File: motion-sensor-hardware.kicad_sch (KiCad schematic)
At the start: 39 parts, among them J1 MX128-2.54-04P-GN01-Cu-Y-A, J2 MX128-2.54-02P-GN01-Cu-Y-A, J3 PZ254V-11-03P, J5 TYPE-C 16PIN 2MD(073), Q1 BSS138, Q2 XR30P10L, SW1 TS-1088-AR02016, SW2 TS-1088-AR02016, U1 ESP32-C3-MINI-1-N4, U2 LD2410C, U5 ASSR-1218

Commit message: Ready to restart work!
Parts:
- removed Q1: BSS138, Package_TO_SOT_SMD:SOT-23, symbol Transistor_FET:BSS138
- removed R13: 10k, Capacitor_SMD:C_0805_2012Metric, symbol Device:R

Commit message: Schematic complete (I think)
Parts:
- removed C10: 10u, Capacitor_SMD:C_0805_2012Metric, symbol Device:C
- removed C7: 1u, Capacitor_SMD:C_0805_2012Metric, symbol Device:C
- removed C8, C9: 0.1u, Capacitor_SMD:C_0805_2012Metric, symbol Device:C
- removed D1, D2: LESD5D5.0CT1G, Diode_SMD:D_SOD-523, symbol Device:D_TVS
- removed D4, D6: P6SMB6.8CA/TR13, Diode_SMD:D_SMB_Handsoldering, symbol Device:D_TVS
- removed D8: BZT52C15S, Diode_SMD:D_SOD-323, symbol Device:D_Zener
- removed Q2: XR30P10L, Package_TO_SOT_SMD:SOT-23, symbol Transistor_FET:Q_PMOS_GSD
- removed R1, R5: 5.1k, Capacitor_SMD:C_0805_2012Metric, symbol Device:R
- removed R10, R9: 0, Capacitor_SMD:C_0805_2012Metric, symbol Device:R
- removed R11, R15, R6, R7, R8: 10k, Capacitor_SMD:C_0805_2012Metric, symbol Device:R
- removed R12: 330, Resistor_SMD:R_0805_2012Metric_Pad1.20x1.40mm_HandSolder, symbol Device:R
- removed R14: 100, Capacitor_SMD:C_0805_2012Metric, symbol Device:R
- added C1: 10uF, Capacitor_SMD:C_0603_1608Metric, symbol !Capacitor-0603:10uF_X5R_10V
- added C14, C8, C9: 100nF, Capacitor_SMD:C_0603_1608Metric, symbol !Capacitor-0603:100nF_X7R_50V
- added C7: 1uF, Capacitor_SMD:C_0603_1608Metric, symbol !Capacitor-0603:1uF_X5R_50V
- added D1: BZT52C10S, Diode_SMD:D_SOD-323, symbol !Diode-Zener:BZT52C10S
- added D2, D3: SMF6.5CA, Diode_SMD:D_SOD-123F, symbol !Circuit Protection-ESD+TVS:SMF6.5CA
- added Q1: AO3401A, Package_TO_SOT_SMD:TSOT-23, symbol !MOSFET:AO3401A
- added R1, R5: 5.1kΩ, Resistor_SMD:R_0603_1608Metric, symbol !Resistor-0603:5.1kΩ
- added R10, R9: 0Ω, Resistor_SMD:R_0603_1608Metric, symbol !Resistor-0603:0Ω
- added R11, R15, R6, R7, R8: 10kΩ, Resistor_SMD:R_0603_1608Metric, symbol !Resistor-0603:10kΩ
- added R12: 330Ω, Resistor_SMD:R_0603_1608Metric, symbol !Resistor-0603:330Ω
- added R14: 100Ω, Resistor_SMD:R_0603_1608Metric, symbol !Resistor-0603:100Ω
- added U6: USBLC6-2SC6, Package_TO_SOT_SMD:SOT-23-6, symbol !Circuit Protection-ESD+TVS:USBLC6-2SC6
- added U7: SN74LV1T125DCK, Package_TO_SOT_SMD:SOT-353_SC-70-5, symbol !Logic-Buffer:SN74LV1T125DCK
- D5: symbol Device:D_TVS -> !Circuit Protection-ESD+TVS:P6SMB24CA-E3/52
- D7: value WS2812B -> WS2812B-HS01/W; symbol LED:WS2812B -> !Optoelectronics-LED:WS2812B-HS01/W; JLCPCB (none) -> C22371521
- F1: symbol Device:Polyfuse -> !Circuit Protection-Resettable Fuse:JK-nSMD100/16V
- J1: value MX128-2.54-04P-GN01-Cu-Y-A -> MX128-2.54-04P; symbol Connector:Screw_Terminal_01x04 -> !Connectors-Screw:MX128-2.54-04P
- J2: value MX128-2.54-02P-GN01-Cu-Y-A -> MX128-2.54-02P; symbol Connector:Screw_Terminal_01x02 -> !Connectors-Screw:MX128-2.54-02P; JLCPCB C5188442 -> C5188442
- J3: symbol Connector_Generic:Conn_01x03 -> !Connectors-Header:PZ254V-11-03P; now not fitted
- J5: symbol Connector:USB_C_Receptacle_USB2.0_16P -> !Connectors-USB:USB_C_Receptacle_USB2.0_16P
- SW1, SW2: symbol Switch:SW_Push -> !Switch:TS-1088-AR02016
- U1: footprint RF_Module:ESP32-C6-MINI-1 -> !RF_Modules:ESP32-C6-MINI-1; symbol motion-sensor-syms:ESP32-C3-MINI-1 -> !RF Modules:ESP32-C3-MINI-1
- U2: footprint HLK:LD2410C -> !Sensors:LD2410C; symbol motion-sensor-syms:LD2410C -> !Sensors:LD2410C
- U5: symbol Relay_SolidState:ASSR-1218 -> !Optoisolator-SSR:ASSR-1218; JLCPCB (none) -> C6747780
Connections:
- net +3.3V: now also C1.1, C8.1, R11.1, R6.1, R7.1, R8.1
- net +5V: now also C14.1, C9.1, U7.5 (VCC)
- net CTL_SW1: now also D2.2 (A2)
- net CTL_SW2: now also D2.1 (A1)
- net GND: now also C1.2, C14.2, C7.2, C8.2, C9.2, D3.1 (A1), R1.2, R15.2, R5.2, U6.2 (GND), U7.1 (~{OE}), U7.3 (GND)
- net LED: now also U7.2 (A)
- net STAT_SW: now also D3.2 (A2)
- net SWON: now also R12.1
- net USB+: now also R10.2
- net USB-: now also R9.2
- net USB1+: now also R10.1, U6.4 (I/O2); no longer J5.A6 (D+), J5.B6 (D+)
- net USB1-: now also R9.1, U6.6 (I/O1); no longer J5.A7 (D-), J5.B7 (D-)
- net VIN: now also D1.1 (K), Q1.2 (S)
- net at J5.A5 (CC1): now also R1.1
- net at SW2.2, U1.8 (EN/CHIP_PU): now also C7.1, R6.2
- net at D7.4 (DIN): now also U7.4 (Y)
- net at U1.22 (GPIO8): now also R8.2
- net at SW1.2, U1.23 (GPIO9): now also R11.2
- net at U1.5 (GPIO2/ADC1_CH2): now also R7.2
- net at J5.B5 (CC2): now also R5.1
- net at D5.2 (A2), F1.2: now also Q1.3 (D)
- net at U5.1: now also R12.2
- net at J5.A4 (VBUS), J5.A9 (VBUS), J5.B4 (VBUS)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: now also U6.5 (VBUS)
- new net: Q1.1 (G), R14.1
- new net: D1.2 (A), R14.2, R15.1
- new net: J5.A7 (D-), J5.B7 (D-), U6.1 (I/O1)
- new net: J5.A6 (D+), J5.B6 (D+), U6.3 (I/O2)
- no-connect marks 6 -> 5
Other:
- note added: "V_{in} is 16 V max"
- moved on the sheet: SW1, SW2

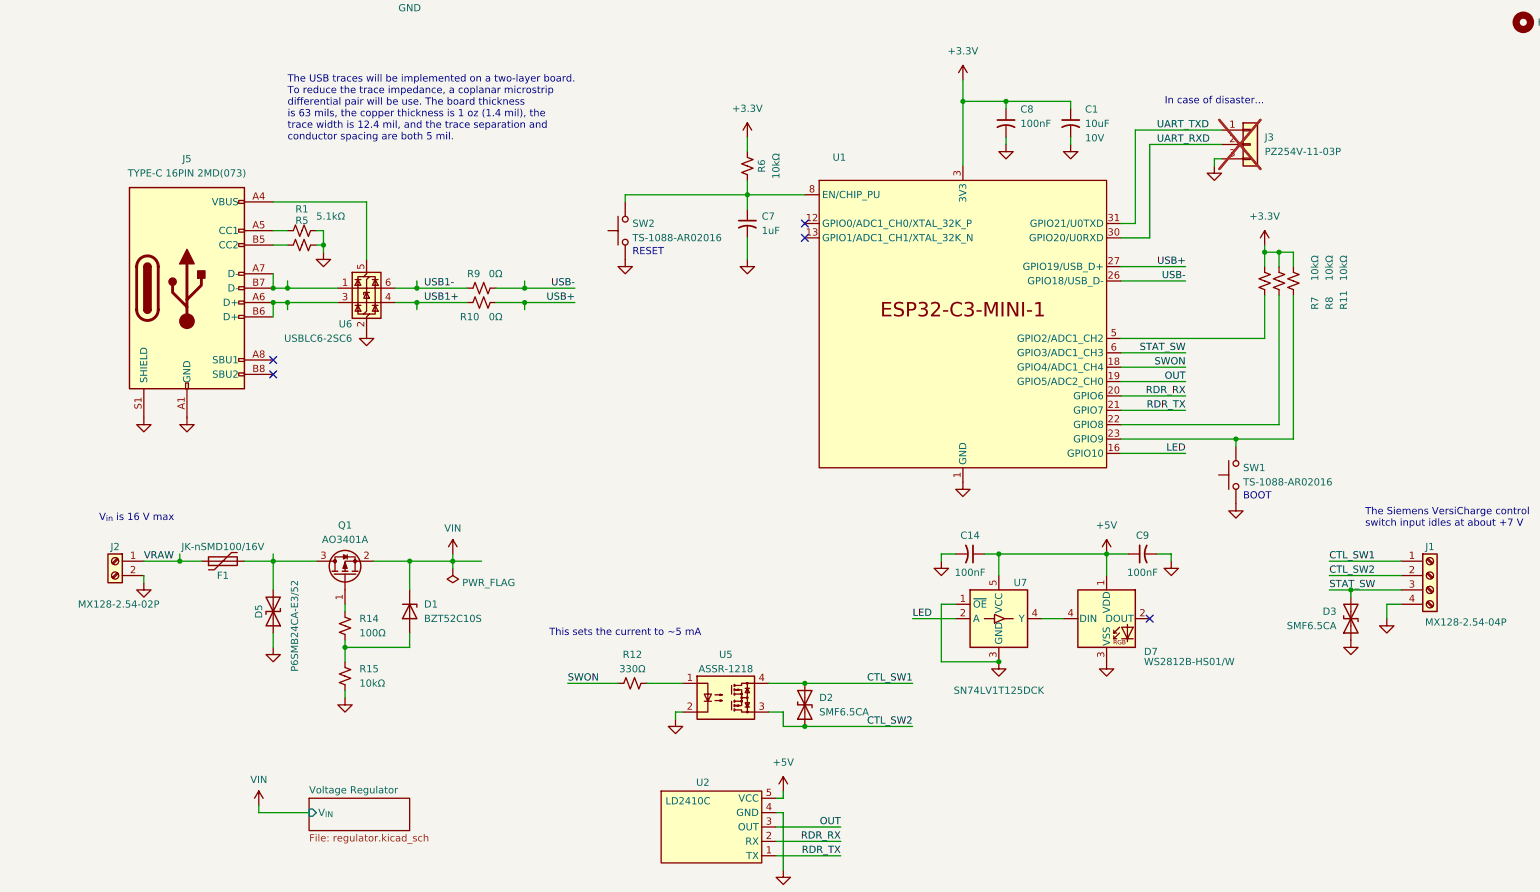
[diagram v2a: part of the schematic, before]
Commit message: Split the two ground planes
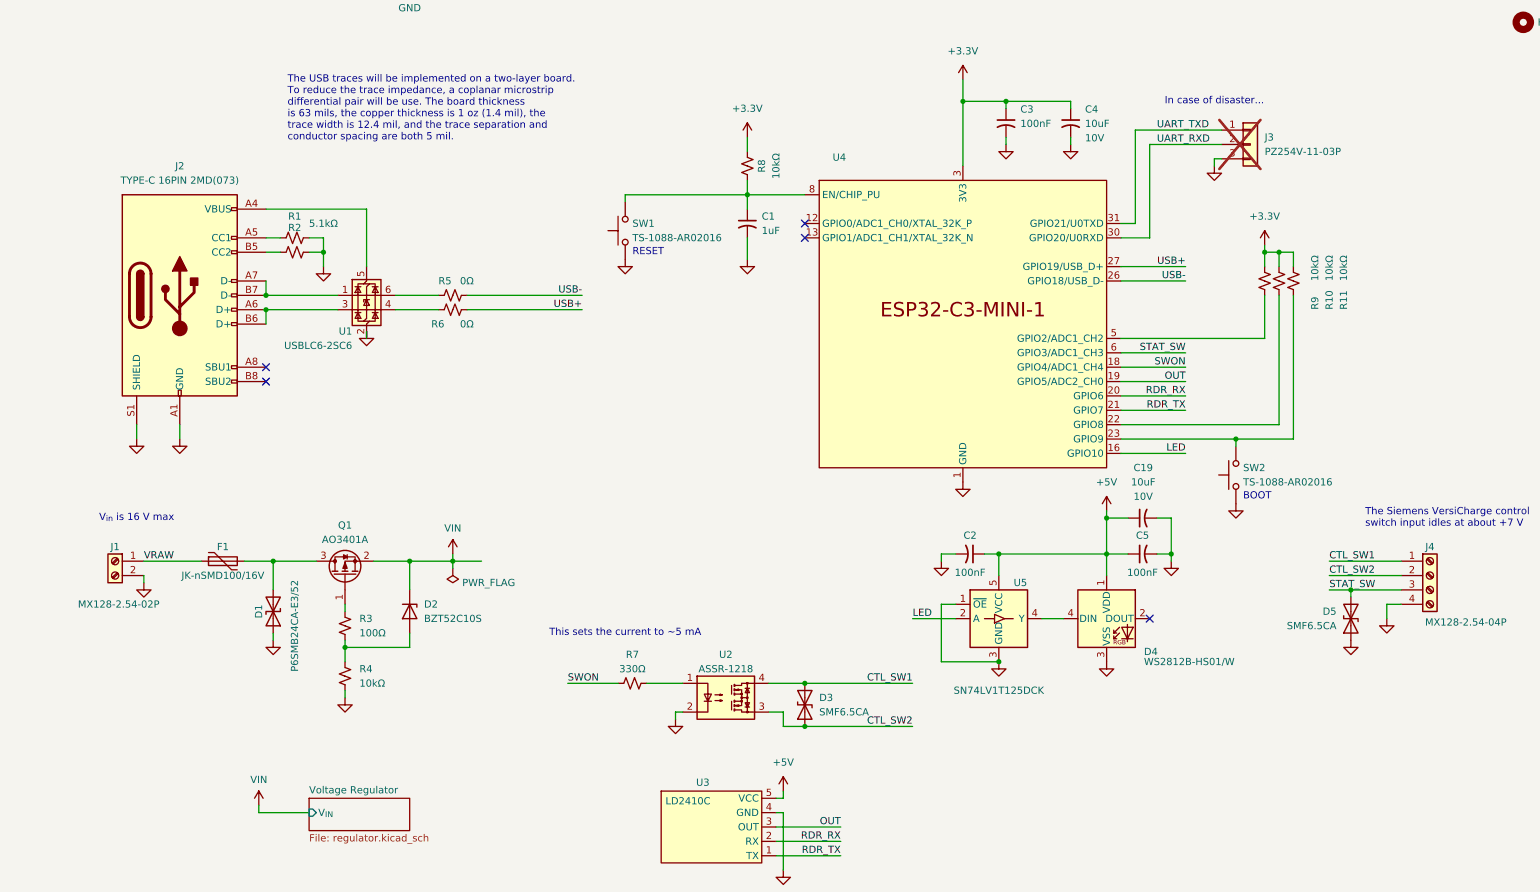
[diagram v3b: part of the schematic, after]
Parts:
- added C19: 10uF, Capacitor_SMD:C_0603_1608Metric, symbol !Capacitor-0603:10uF_X5R_10V
- J1: renamed from J2; footprint My_Connectors:MX300-5.0-02P -> !Connectors:MX128-2.54-02P
- J4: renamed from J1; footprint (none) -> !Connectors:MX128-2.54-04P
- renumbered C7 to C1, C14 to C2, C8 to C3, C1 to C4, C9 to C5, D5 to D1, D1 to D2, D2 to D3, D7 to D4, D3 to D5, J5 to J2, R8 to R10, R5 to R2, R14 to R3, R15 to R4, R9 to R5, R10 to R6, R12 to R7, R6 to R8, R7 to R9, SW2 to SW1, SW1 to SW2, U6 to U1, U5 to U2, U2 to U3, U1 to U4, U7 to U5
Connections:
- net +5V: now also C19.1
- net GND: now also C19.2
- net USB1+: no longer names the net of R6.1, U1.4 (I/O2)
- net USB1-: no longer names the net of R5.1, U1.6 (I/O1)
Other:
- moved on the sheet: J2, R1, R2, R5, R6, U1

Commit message: Rev B Submitted
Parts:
- removed D1: P6SMB24CA-E3/52, Diode_SMD:D_SMB, symbol !Circuit Protection-ESD+TVS:P6SMB24CA-E3/52
- added D1: SMBJ16CA, Diode_SMD:D_SMB, symbol !Circuit Protection-ESD+TVS:SMBJ16CA
- C1: JLCPCB C15849 -> (none); JLCPCB PN (none) -> C15849
- C19, C4: JLCPCB C19702 -> (none); JLCPCB PN (none) -> C19702
- C2, C3, C5: JLCPCB C14663 -> (none); JLCPCB PN (none) -> C14663
- D2: JLCPCB C19077446 -> (none); JLCPCB PN (none) -> C19077446
- D3, D5: JLCPCB C19077501 -> (none); JLCPCB PN (none) -> C19077501
- D4: JLCPCB C22371521 -> (none); JLCPCB PN (none) -> C22371521
- F1: JLCPCB C2830246 -> (none); JLCPCB PN (none) -> C2830246
- J1: FT Rotation Offset (none) -> 180; JLCPCB C5188442 -> (none); JLCPCB PN (none) -> C5188442
- J2: FT Origin (none) -> Center; JLCPCB C2765186 -> (none); JLCPCB PN (none) -> C2765186
- J3: JLCPCB C2937625 -> (none); JLCPCB PN (none) -> C2937625
- J4: FT Rotation Offset (none) -> 180; JLCPCB C5188444 -> (none); JLCPCB PN (none) -> C5188444
- Q1: JLCPCB C15127 -> (none); JLCPCB PN (none) -> C15127
- R1, R2: JLCPCB C23186 -> (none); JLCPCB PN (none) -> C23186
- R10, R11, R4, R8, R9: JLCPCB C25804 -> (none); JLCPCB PN (none) -> C25804
- R3: JLCPCB C22775 -> (none); JLCPCB PN (none) -> C22775
- R5, R6: JLCPCB C21189 -> (none); JLCPCB PN (none) -> C21189
- R7: JLCPCB C23138 -> (none); JLCPCB PN (none) -> C23138
- SW1, SW2: JLCPCB C720477 -> (none); JLCPCB PN (none) -> C720477
- U1: FT Rotation Offset (none) -> 90; JLCPCB C7519 -> (none); JLCPCB PN (none) -> C7519
- U2: FT Rotation Offset (none) -> 90; JLCPCB C6747780 -> (none); JLCPCB PN (none) -> C6747780
- U3: JLCPCB C19723500 -> (none); JLCPCB PN (none) -> C19723500
- U4: JLCPCB C2838502 -> (none); JLCPCB PN (none) -> C2838502
- U5: FT Rotation Offset (none) -> 180; JLCPCB C75925 -> (none); JLCPCB PN (none) -> C75925
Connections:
- net GND: now also D1.1 (A1)
- net at F1.2, Q1.3 (D): now also D1.2 (A2)
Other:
- title: (none) -> Motion Sensor/Charge Control

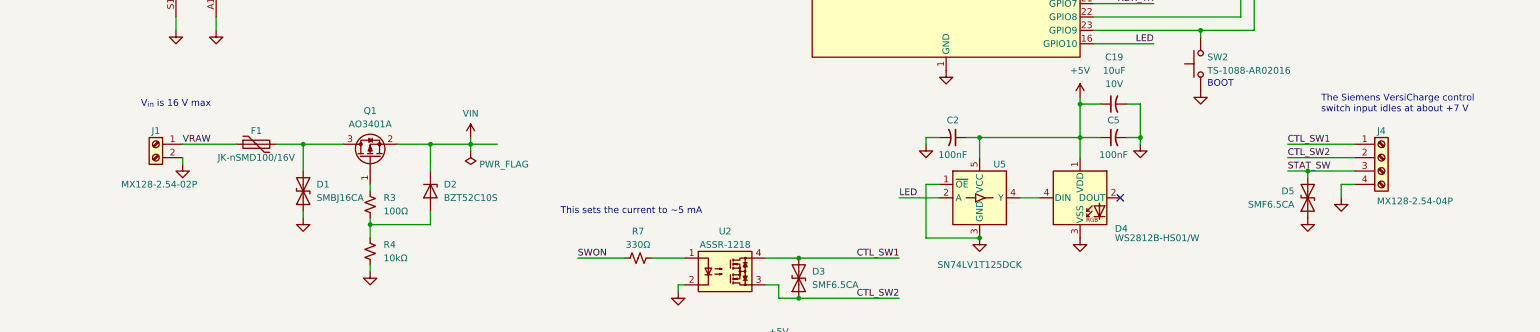
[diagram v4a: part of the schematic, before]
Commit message: Fixed screw term pin 1 issue
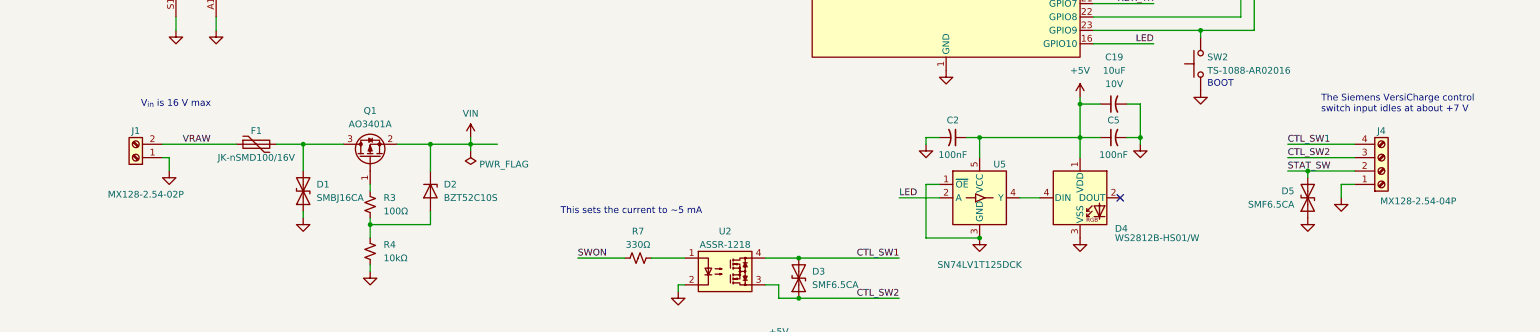
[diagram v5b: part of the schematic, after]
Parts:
- SW1, SW2: footprint Button_Switch_SMD:SW_Push_SPST_NO_Alps_SKRK -> !Switches:SW_TS-1088-xx020xx_XUNPU
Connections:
- net CTL_SW1: now also J4.4 (Pin_4); no longer J4.1 (Pin_1)
- net CTL_SW2: now also J4.3 (Pin_3); no longer J4.2 (Pin_2)
- net GND: now also J1.1 (Pin_1), J4.1 (Pin_1); no longer J1.2 (Pin_2), J4.4 (Pin_4)
- net STAT_SW: now also J4.2 (Pin_2); no longer J4.3 (Pin_3)
- net VRAW: now also J1.2 (Pin_2); no longer J1.1 (Pin_1)
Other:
- moved on the sheet: J1
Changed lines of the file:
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@@
 	(wire
 		(pts
+			(xy 25.4 138.43) (xy 39.37 138.43)
+		)
+		(stroke
+			(width 0)
+			(type default)
+		)
+	)
+	(wire
+		(pts
 			(xy 201.93 104.14) (xy 213.36 104.14)
 		)
@@
 	(wire
 		(pts
-			(xy 29.21 140.97) (xy 29.21 142.24)
-		)
-		(stroke
-			(width 0)
-			(type default)
-		)
-	)
-	(wire
-		(pts
 			(xy 64.77 146.05) (xy 64.77 147.32)
 		)
@@
 	(wire
 		(pts
-			(xy 142.24 180.34) (xy 142.24 179.07)
+			(xy 25.4 140.97) (xy 26.67 140.97)
 		)
 		(stroke
@@
 	(wire
 		(pts
-			(xy 29.21 138.43) (xy 39.37 138.43)
+			(xy 142.24 180.34) (xy 142.24 179.07)
 		)
 		(stroke
@@
 	(wire
 		(pts
+			(xy 26.67 140.97) (xy 26.67 143.51)
+		)
+		(stroke
+			(width 0)
+			(type default)
+		)
+	)
+	(wire
+		(pts
 			(xy 227.33 83.82) (xy 229.87 83.82)
 		)
@@
 			)
 		)
-		(property "Footprint" "Button_Switch_SMD:SW_Push_SPST_NO_Alps_SKRK"
+		(property "Footprint" "!Switches:SW_TS-1088-xx020xx_XUNPU"
 			(at 109.22 80.01 0)
 			(effects
@@
 	(symbol
 		(lib_id "!Connectors-Screw:MX128-2.54-02P")
-		(at 24.13 138.43 0)
-		(mirror y)
+		(at 20.32 140.97 180)
 		(unit 1)
 		(exclude_from_sim no)
@@
 		(dnp no)
 		(property "Reference" "J1"
-			(at 24.13 135.89 0)
+			(at 20.32 135.89 0)
 			(effects
 				(font
@@
 		)
 		(property "Value" "MX128-2.54-02P"
-			(at 24.765 146.05 0)
+			(at 22.225 147.955 0)
 			(effects
 				(font
@@
 		)
 		(property "Footprint" "!Connectors:MX128-2.54-02P"
-			(at 24.13 138.43 0)
+			(at 20.32 140.97 0)
 			(effects
 				(font
@@
 		)
 		(property "Datasheet" "https://jlcpcb.com/api/file/downloadByFileSystemAccessId/8604752379715997696"
-			(at 24.13 138.43 0)
+			(at 20.32 140.97 0)
 			(effects
 				(font
@@
 		)
 		(property "Description" "Screw Term Block, 2 Pos, 2.54 mm"
-			(at 24.13 138.43 0)
+			(at 20.32 140.97 0)
 			(effects
 				(font
@@
 		)
 		(property "JLCPCB PN" "C5188442"
-			(at 24.13 138.43 0)
+			(at 20.32 140.97 0)
 			(effects
 				(font
@@
 		)
 		(property "FT Rotation Offset" "180"
-			(at 24.13 138.43 0)
+			(at 20.32 140.97 0)
 			(effects
 				(font
@@
 		)
 		(instances
-			(project ""
+			(project "motion-sensor-hardware"
 				(path "/d999e802-7382-49ed-b28b-80393e8497d9"
 					(reference "J1")
@@
 			)
 		)
-		(property "Footprint" "Button_Switch_SMD:SW_Push_SPST_NO_Alps_SKRK"
+		(property "Footprint" "!Switches:SW_TS-1088-xx020xx_XUNPU"
 			(at 217.17 123.19 0)
 			(effects
@@
 	(symbol
 		(lib_id "!Connectors-Screw:MX128-2.54-04P")
-		(at 256.54 140.97 0)
+		(at 256.54 143.51 0)
+		(mirror x)
 		(unit 1)
 		(exclude_from_sim no)
@@
 		)
 		(property "Value" "MX128-2.54-04P"
-			(at 262.89 149.225 0)
+			(at 263.525 149.225 0)
 			(effects
 				(font
@@
 		)
 		(property "Footprint" "!Connectors:MX128-2.54-04P"
-			(at 256.54 140.97 0)
+			(at 256.54 143.51 0)
 			(effects
 				(font
@@
 		)
 		(property "Datasheet" "https://jlcpcb.com/api/file/downloadByFileSystemAccessId/8604752386087010304"
-			(at 256.54 140.97 0)
+			(at 256.54 143.51 0)
 			(effects
 				(font
@@
 		)
 		(property "Description" "Screw Term Block, 4 Pos, 2.54mm"
-			(at 256.54 140.97 0)
+			(at 256.54 143.51 0)
 			(effects
 				(font
@@
 		)
 		(property "JLCPCB PN" "C5188444"
-			(at 256.54 140.97 0)
+			(at 256.54 143.51 0)
 			(effects
 				(font
@@
 		)
 		(property "FT Rotation Offset" "180"
-			(at 256.54 140.97 0)
+			(at 256.54 143.51 0)
 			(effects
 				(font
@@
 		)
 		(instances
-			(project ""
+			(project "motion-sensor-hardware"
 				(path "/d999e802-7382-49ed-b28b-80393e8497d9"
 					(reference "J4")
@@
 	(symbol
 		(lib_id "power:GND")
-		(at 29.21 142.24 0)
+		(at 26.67 143.51 0)
 		(unit 1)
 		(exclude_from_sim no)
@@
 		(dnp no)
 		(property "Reference" "#PWR02"
-			(at 29.21 148.59 0)
+			(at 26.67 149.86 0)
 			(effects
 				(font
@@
 		)
 		(property "Value" "GND"
-			(at 29.21 146.05 0)
+			(at 26.67 147.32 0)
 			(effects
 				(font
@@
 		)
 		(property "Footprint" ""
-			(at 29.21 142.24 0)
+			(at 26.67 143.51 0)
 			(effects
 				(font
@@
 		)
 		(property "Datasheet" ""
-			(at 29.21 142.24 0)
+			(at 26.67 143.51 0)
 			(effects
 				(font
@@
 		)
 		(property "Description" "Power symbol creates a global label with name \"GND\" , ground"
-			(at 29.21 142.24 0)
+			(at 26.67 143.51 0)
 			(effects
 				(font
